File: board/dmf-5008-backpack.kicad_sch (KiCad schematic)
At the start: 58 parts, among them J1 5V IN, J2 3V3 IN, J3 BOOST, J4 Barrel_Jack_Switch, P1 CONN_01X25, Q1 BSS138, Q10 BSS138, Q11 BSS138, Q12 BSS138, Q13 BSS138, Q14 BSS138, Q2 BSS138, Q3 BSS138, Q4 BSS138, Q5 BSS138, Q6 BSS138, Q7 BSS138, Q8 BSS138, SW1 RESET, U1 Pico, U2 MIC4830

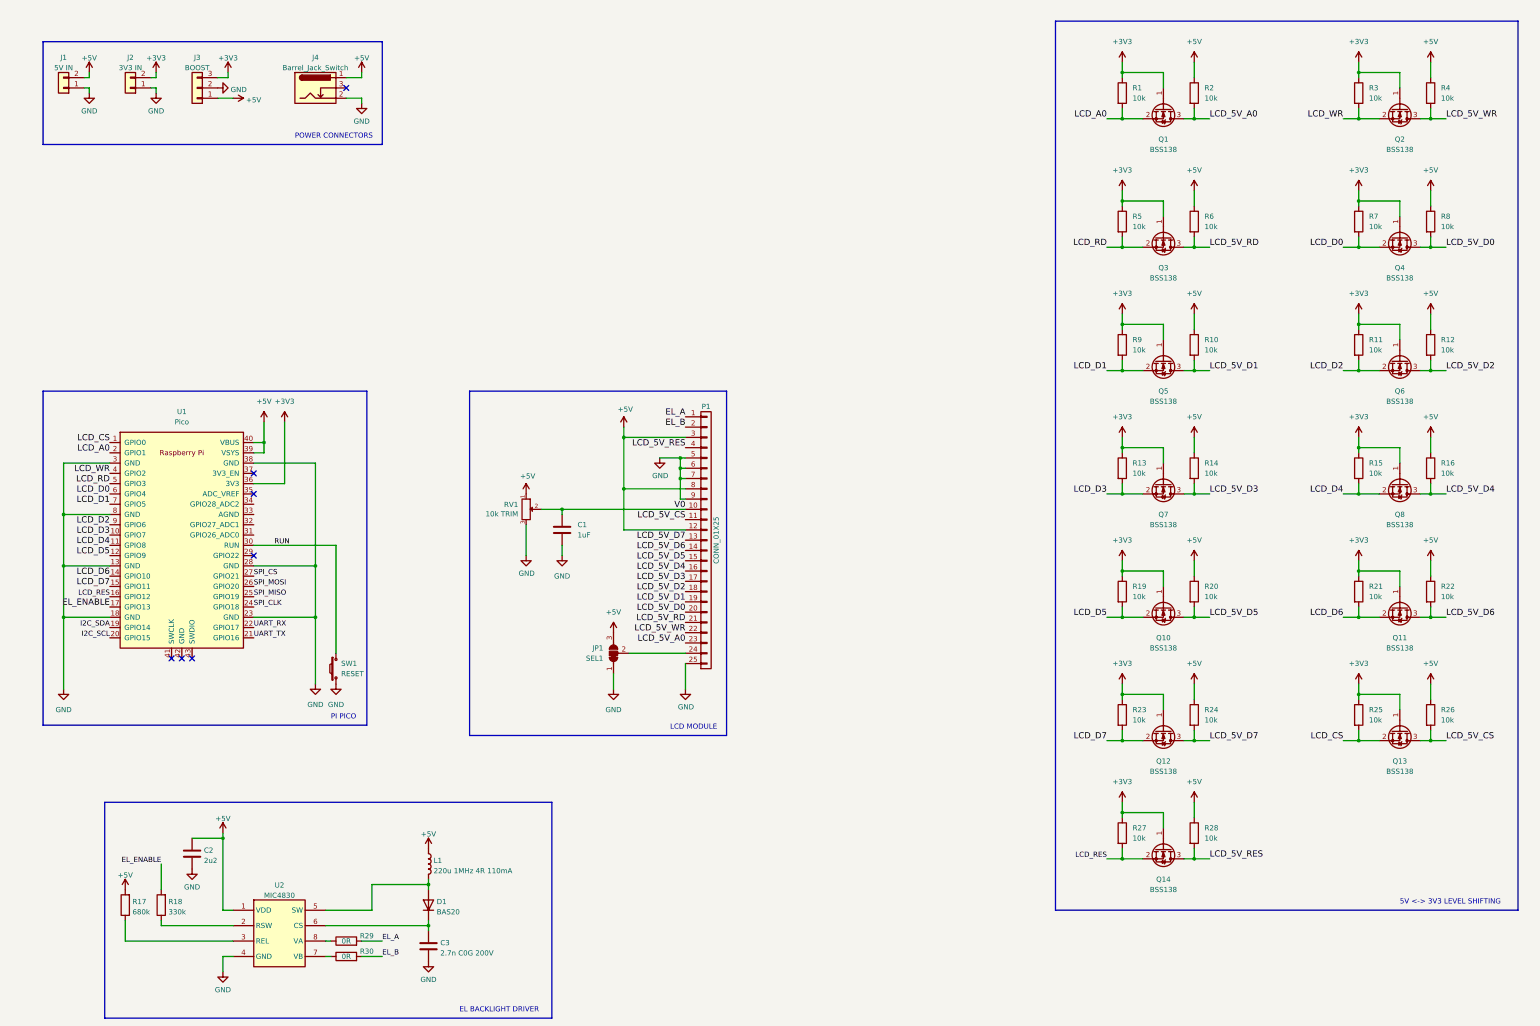
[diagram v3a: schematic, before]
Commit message: Finish schematic, setup board capabilities
* Finish schematic to checklist, happy with ERC
    * Add data connections and I2C pullups
    * Make EL_ENABLE an NPN pulldown, otherwise things will be confusing
      if R_SW is only pulled up to 3v3 by a GPIO.
    * Choose an inductor for the EL driver
* Rough final placement of PCB
* Setup PCB capabilities/tracks/vias to JLC's numbers
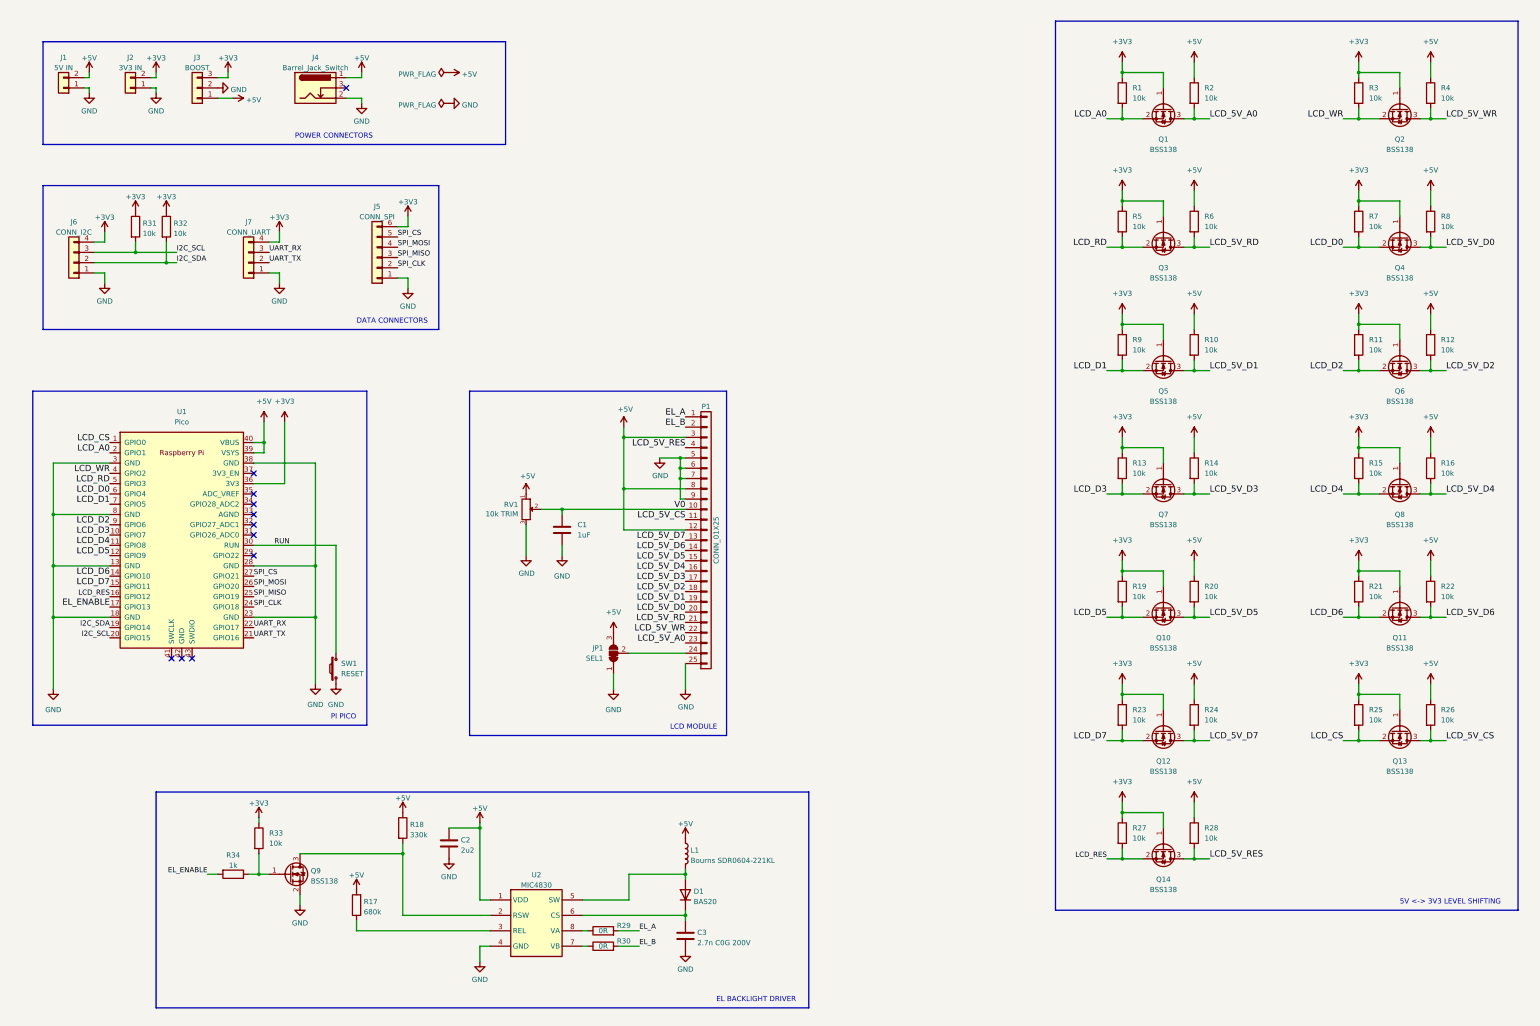
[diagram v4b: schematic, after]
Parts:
- added J5: CONN_SPI, Connector_PinHeader_2.54mm:PinHeader_1x06_P2.54mm_Vertical, symbol Connector_Generic:Conn_01x06
- added J6: CONN_I2C, Connector_PinHeader_2.54mm:PinHeader_1x04_P2.54mm_Vertical, symbol Connector_Generic:Conn_01x04
- added J7: CONN_UART, Connector_PinHeader_2.54mm:PinHeader_1x04_P2.54mm_Vertical, symbol Connector_Generic:Conn_01x04
- added Q9: BSS138, Package_TO_SOT_SMD:SOT-23, symbol Transistor_FET:BSS138
- added R31, R32: 10k, Resistor_SMD:R_0603_1608Metric, symbol Device:R
- added R33: 10k, Resistor_SMD:R_0603_1608Metric, symbol device:R
- added R34: 1k, Resistor_SMD:R_0603_1608Metric, symbol Device:R
- L1: value 220u 1MHz 4R 110mA -> Bourns SDR0604-221KL; footprint (none) -> Inductor_SMD:L_Bourns_SRN6045TA
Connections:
- net +3V3: now also J5.6 (Pin_6), J6.4 (Pin_4), J7.4 (Pin_4), R31.1, R32.1, R33.1
- net +5V: now also R18.1
- net EL_ENABLE: now also R34.2; no longer R18.2
- net GND: now also J5.1 (Pin_1), J6.1 (Pin_1), J7.1 (Pin_1), Q9.2 (S)
- net I2C_SCL: now also J6.3 (Pin_3), R31.2
- net I2C_SDA: now also J6.2 (Pin_2), R32.2
- net SPI_CLK: now also J5.2 (Pin_2)
- net SPI_CS: now also J5.5 (Pin_5)
- net SPI_MISO: now also J5.3 (Pin_3)
- net SPI_MOSI: now also J5.4 (Pin_4)
- net UART_RX: now also J7.3 (Pin_3)
- net UART_TX: now also J7.2 (Pin_2)
- net at U2.2 (RSW): now also R18.2, Q9.3 (D); no longer R18.1
- new net: Q9.1 (G), R33.2, R34.1
- no-connect marks 7 -> 11
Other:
- note added: "DATA CONNECTORS"
- moved on the sheet: C2, C3, D1, L1, R17, R18, R29, R30, U2

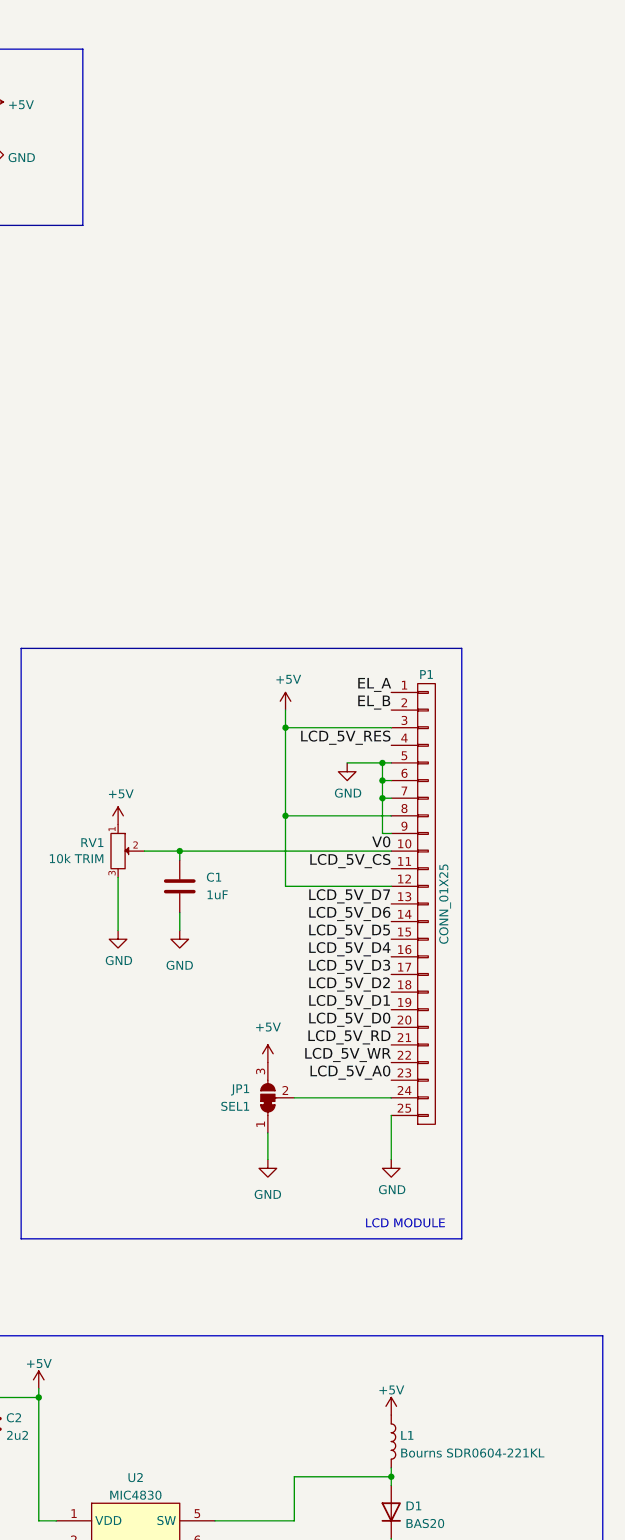
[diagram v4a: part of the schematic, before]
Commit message: PCB finished except for final checking
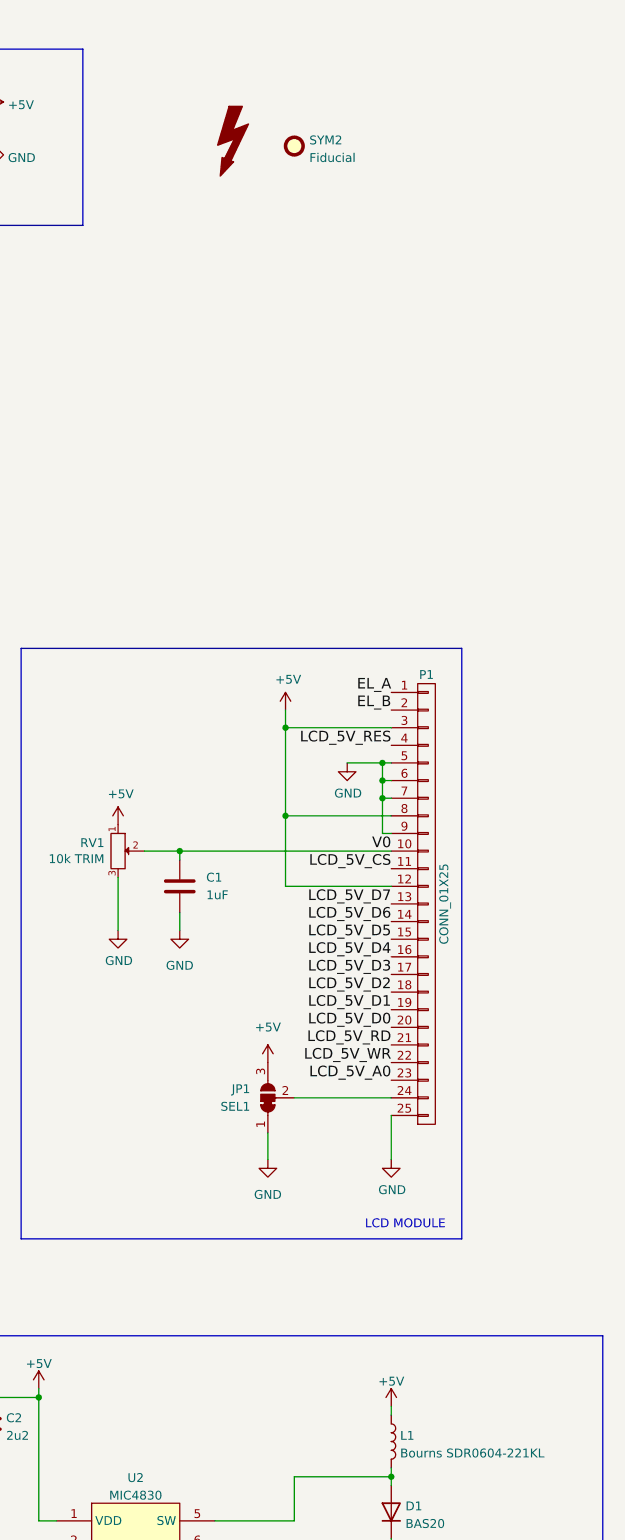
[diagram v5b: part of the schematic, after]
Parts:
- added SYM1: SYM_Flash_Large, Symbol:Symbol_Highvoltage_Type2_CopperTop_Small, symbol Graphic:SYM_Flash_Large
- added SYM2: Fiducial, Symbol:Symbol_Barrel_Polarity, symbol Mechanical:Fiducial
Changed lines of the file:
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@@
+    (stroke (width 0) (type default) (color 0 0 0 0))
+  )
+  (wire (pts (xy 191.77 222.25) (xy 191.77 223.52))
     (stroke (width 0) (type default) (color 0 0 0 0))
   )
@@
     (pin "2")
   )
-  (symbol (lib_id "power:+5V") (at 191.77 223.52 0) (unit 1)
-    (in_bom yes) (on_board yes) (fields_autoplaced)
-    (property "Reference" "#PWR011" (id 0) (at 191.77 227.33 0)
-      (effects (font (size 1.27 1.27)) hide)
-    )
-    (property "Value" "+5V" (id 1) (at 191.77 219.9442 0))
-    (property "Footprint" "" (id 2) (at 191.77 223.52 0)
-      (effects (font (size 1.27 1.27)) hide)
-    )
-    (property "Datasheet" "" (id 3) (at 191.77 223.52 0)
+  (symbol (lib_id "power:+5V") (at 191.77 222.25 0) (unit 1)
+    (in_bom yes) (on_board yes) (fields_autoplaced)
+    (property "Reference" "#PWR011" (id 0) (at 191.77 226.06 0)
+      (effects (font (size 1.27 1.27)) hide)
+    )
+    (property "Value" "+5V" (id 1) (at 191.77 218.6742 0))
+    (property "Footprint" "" (id 2) (at 191.77 222.25 0)
+      (effects (font (size 1.27 1.27)) hide)
+    )
+    (property "Datasheet" "" (id 3) (at 191.77 222.25 0)
       (effects (font (size 1.27 1.27)) hide)
     )
@@
     )
     (pin "1")
+  )
+  (symbol (lib_id "Mechanical:Fiducial") (at 177.8 40.64 0) (unit 1)
+    (in_bom yes) (on_board yes) (fields_autoplaced)
+    (property "Reference" "SYM2" (id 0) (at 179.959 39.8053 0)
+      (effects (font (size 1.27 1.27)) (justify left))
+    )
+    (property "Value" "Fiducial" (id 1) (at 179.959 42.3422 0)
+      (effects (font (size 1.27 1.27)) (justify left))
+    )
+    (property "Footprint" "Symbol:Symbol_Barrel_Polarity" (id 2) (at 177.8 40.64 0)
+      (effects (font (size 1.27 1.27)) hide)
+    )
+    (property "Datasheet" "~" (id 3) (at 177.8 40.64 0)
+      (effects (font (size 1.27 1.27)) hide)
+    )
   )
   (symbol (lib_id "power:+3V3") (at 358.14 93.98 0) (unit 1)
@@
     (pin "3")
   )
+  (symbol (lib_id "Graphic:SYM_Flash_Large") (at 168.91 39.37 0) (unit 1)
+    (in_bom yes) (on_board yes) (fields_autoplaced)
+    (property "Reference" "SYM1" (id 0) (at 165.1 39.37 90)
+      (effects (font (size 1.27 1.27)) hide)
+    )
+    (property "Value" "SYM_Flash_Large" (id 1) (at 172.212 39.37 90)
+      (effects (font (size 1.27 1.27)) hide)
+    )
+    (property "Footprint" "Symbol:Symbol_Highvoltage_Type2_CopperTop_Small" (id 2) (at 168.656 41.656 0)
+      (effects (font (size 1.27 1.27)) hide)
+    )
+    (property "Datasheet" "~" (id 3) (at 179.07 41.91 0)
+      (effects (font (size 1.27 1.27)) hide)
+    )
+  )
   (sheet_instances
     (path "/" (page "1"))
@@
       (reference "SW1") (unit 1) (value "RESET") (footprint "Button_Switch_THT:SW_PUSH_6mm")
     )
+    (path "/fcdbcb73-7cda-41ef-b556-2d852c0dbdfa"
+      (reference "SYM1") (unit 1) (value "SYM_Flash_Large") (footprint "Symbol:Symbol_Highvoltage_Type2_CopperTop_Small")
+    )
+    (path "/a02852ff-9177-477b-b814-1cb0a9867076"
+      (reference "SYM2") (unit 1) (value "Fiducial") (footprint "Symbol:Symbol_Barrel_Polarity")
+    )
     (path "/adff25db-76e7-4f54-a91d-4c95aa896a3d"

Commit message: Final checks and fixes
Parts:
- RV1: footprint Potentiometer_THT:Potentiometer_Bourns_3386F_Vertical -> Potentiometer_THT:Potentiometer_ACP_CA9-V10_Vertical
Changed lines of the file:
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@@
       (effects (font (size 1.27 1.27)) (justify right))
     )
-    (property "Footprint" "Potentiometer_THT:Potentiometer_Bourns_3386F_Vertical" (id 2) (at 93.98 -90.17 0)
+    (property "Footprint" "Potentiometer_THT:Potentiometer_ACP_CA9-V10_Vertical" (id 2) (at 93.98 -90.17 0)
       (effects (font (size 1.27 1.27)) hide)
     )
@@
     )
     (path "/00000000-0000-0000-0000-000058a6fe12"
-      (reference "RV1") (unit 1) (value "10k TRIM") (footprint "Potentiometer_THT:Potentiometer_Bourns_3386F_Vertical")
+      (reference "RV1") (unit 1) (value "10k TRIM") (footprint "Potentiometer_THT:Potentiometer_ACP_CA9-V10_Vertical")
     )
     (path "/ab27d000-3ee1-4092-bafb-2d8df5df3cbc"

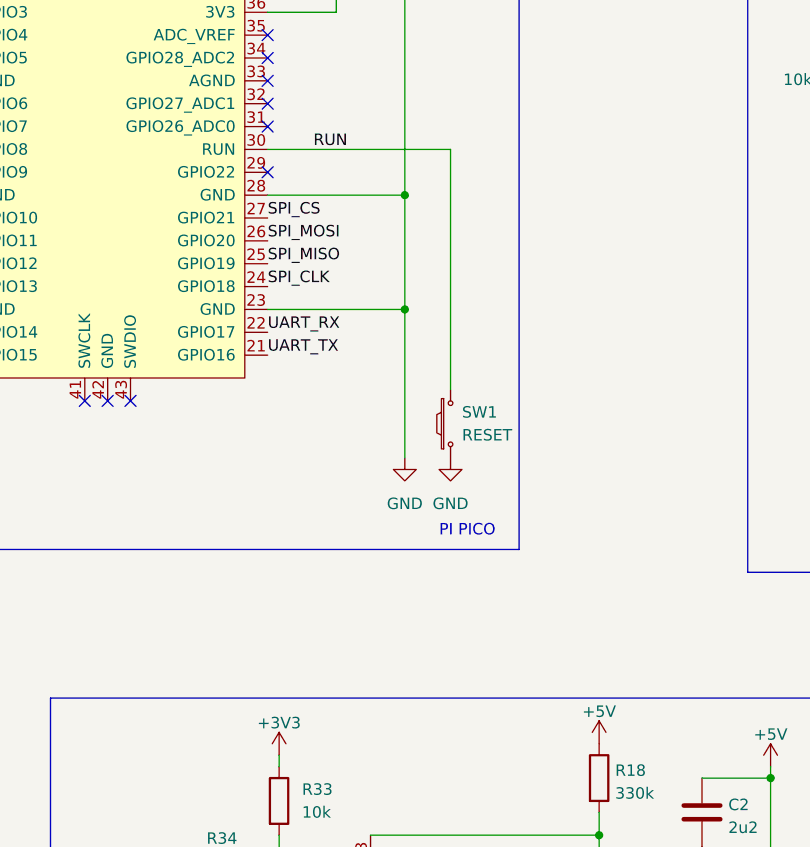
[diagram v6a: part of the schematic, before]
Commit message: Add finalised BOM for PCB
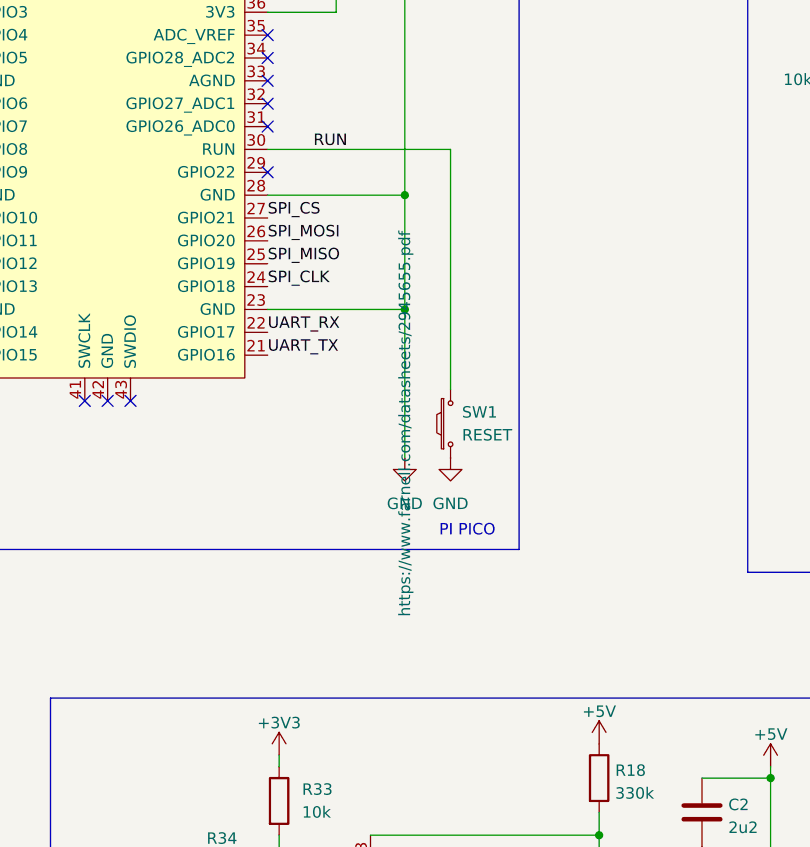
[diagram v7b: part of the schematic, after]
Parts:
- C1: Farnell (none) -> 3013484
- C2: Farnell (none) -> 3013491
- C3: Farnell (none) -> 2210975
- D1: Farnell (none) -> 1081182
- L1: Farnell (none) -> 1828016
- Q1, Q10, Q11, Q12, Q13, Q14, Q2, Q3, Q4, Q5, Q6, Q7, Q8, Q9: Farnell (none) -> 3872309
- R1, R10, R11, R12, R13, R14, R15, R16, R19, R2, R20, R21, R22, R23, R24, R25, R26, R27, R28, R3, R31, R32, R33, R4, R5, R6, R7, R8, R9: Farnell (none) -> 4004520
- R17: Farnell (none) -> 3994573
- R18: Farnell (none) -> 3994550
- R29, R30: Farnell (none) -> 2695115
- R34: Farnell (none) -> 4004543
- SW1: Farnell (none) -> 2543090
